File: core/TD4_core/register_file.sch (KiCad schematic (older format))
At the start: 12 parts

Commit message: Started refactoring
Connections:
- net In_0 renamed In0
- net In_1 renamed In1
- net In_2 renamed In2
- net In_3 renamed In3
- net Out_A_0 renamed A0
- net Out_A_1 renamed A1
- net Out_A_2 renamed A2
- net Out_A_3 renamed A3
- net Out_B_0 renamed B0
- net Out_B_1 renamed B1
- net Out_B_2 renamed B2
- net Out_B_3 renamed B3
- net Out_OUT_0 renamed OUT0
- net Out_OUT_1 renamed OUT1
- net Out_OUT_2 renamed OUT2
- net Out_OUT_3 renamed OUT3
- net Out_PC_0 renamed PC0
- net Out_PC_1 renamed PC1
- net Out_PC_2 renamed PC2
- net Out_PC_3 renamed PC3
- net Reg_sel_0 renamed Reg_sel0
- net Reg_sel_1 renamed Reg_sel1
- net Reg_sel_2 renamed Reg_sel2
- net Reg_sel_3 renamed Reg_sel3
- net nRESET renamed ~RESET
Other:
- note removed: "Reset & Clock"

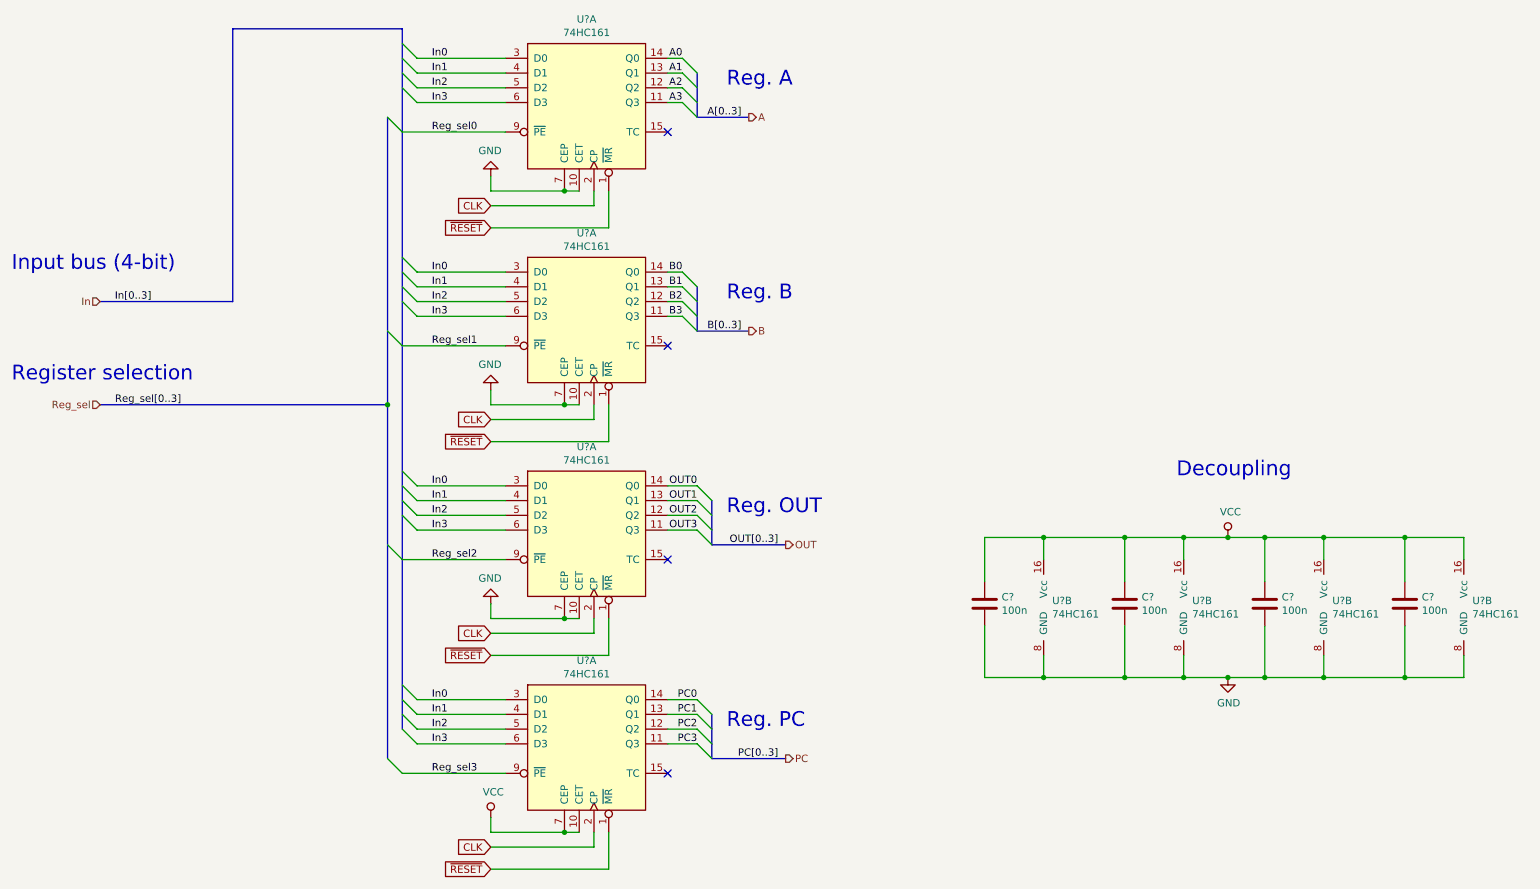
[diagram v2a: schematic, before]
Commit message: Main core schematic done; only decoder left
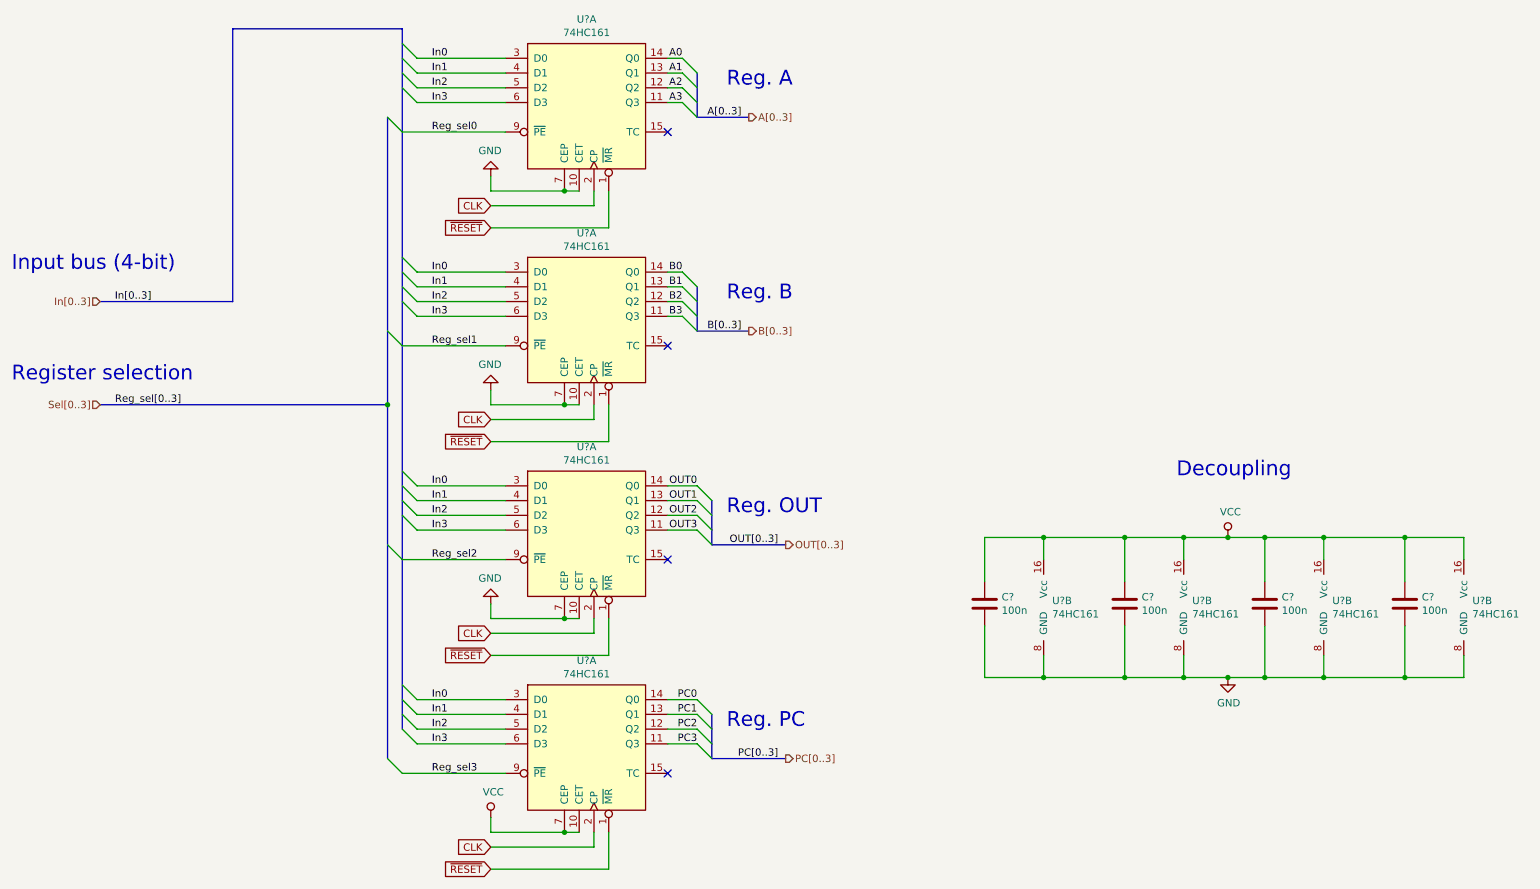
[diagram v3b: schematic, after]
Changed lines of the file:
@@
 $Descr A4 11693 8268
 encoding utf-8
-Sheet 2 6
+Sheet 2 9
 Title "TD4 core module"
 Date ""
@@
 Decoupling
 Text HLabel 5500 1850 2    50   Output ~ 0
-A
+A[0..3]
 Entry Wire Line
 	5050 2900 5150 3000
@@
 	4950 3200 5050 3200
 Text HLabel 5500 3300 2    50   Output ~ 0
-B
+B[0..3]
 Entry Wire Line
 	5150 4350 5250 4450
@@
 	4950 4650 5150 4650
 Text HLabel 5750 4750 2    50   Output ~ 0
-OUT
+OUT[0..3]
 Entry Wire Line
 	5150 5800 5250 5900
@@
 	4950 6100 5150 6100
 Text HLabel 5750 6200 2    50   Output ~ 0
-PC
+PC[0..3]
 Wire Wire Line
 	3750 3900 4450 3900
@@
 	3050 3800 1100 3800
 Text HLabel 1100 3800 0    50   Input ~ 0
-Reg_sel
+Sel[0..3]
 Text Label 1650 3800 2    50   ~ 0
 Reg_sel[0..3]
@@
 In[0..3]
 Text HLabel 1100 3100 0    50   Input ~ 0
-In
+In[0..3]
 Wire Wire Line
 	3250 2900 3850 2900

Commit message: Core assembled; decoder left
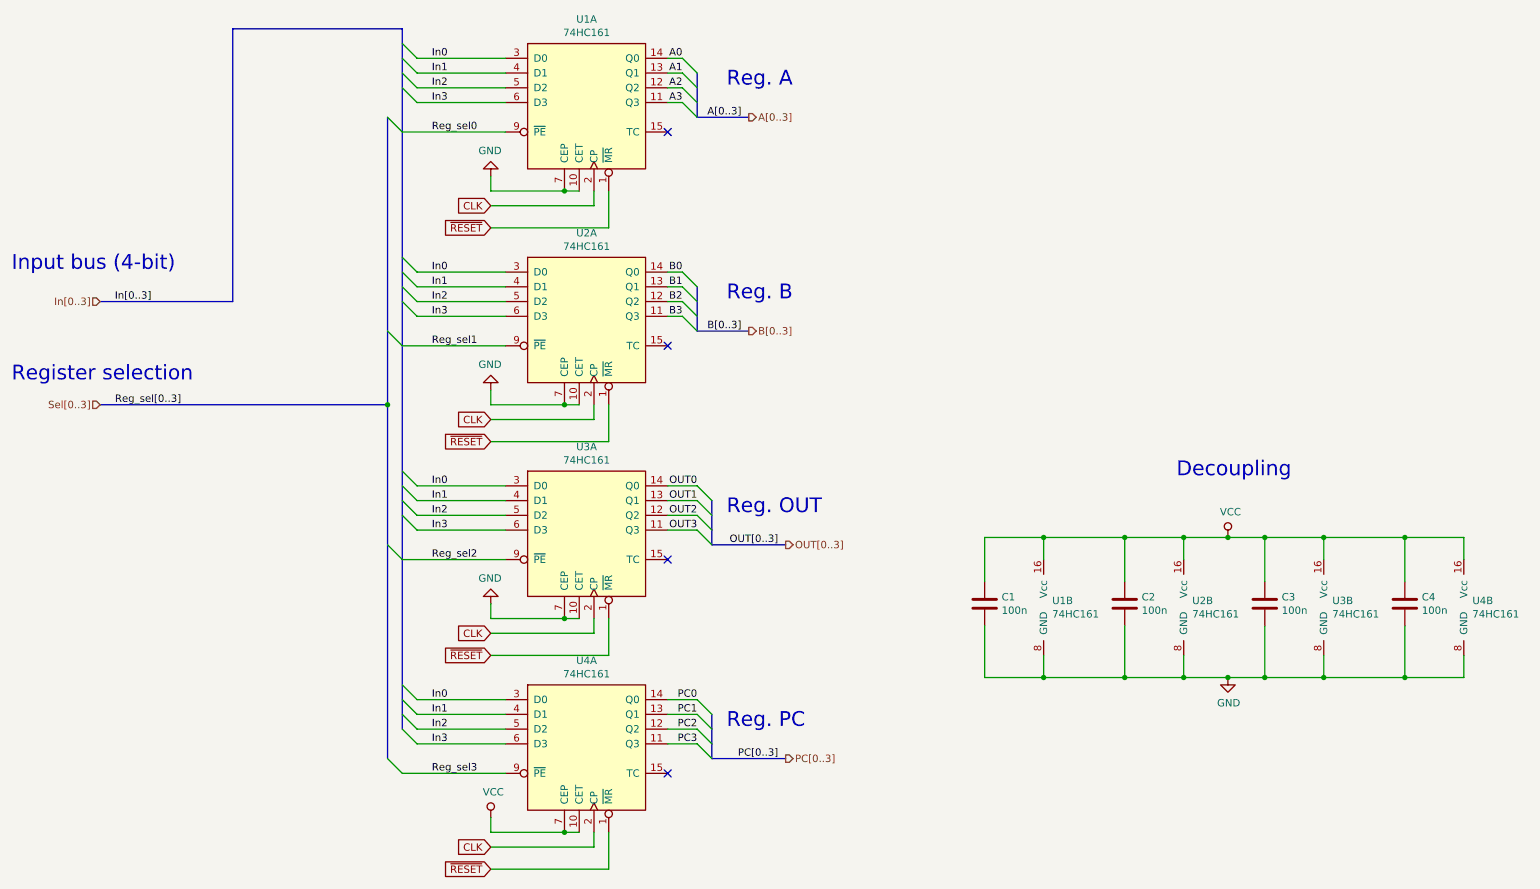
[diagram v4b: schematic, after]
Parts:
- gave numbers to parts that had none: 8
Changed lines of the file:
@@
 P 4400 1800
 AR Path="/5C597F7D" Ref="U?"  Part="1"
-AR Path="/5C594EF5/5C597F7D" Ref="U?"  Part="1"
-F 0 "U?" H 4400 2415 50  0000 C CNN
+AR Path="/5C594EF5/5C597F7D" Ref="U1"  Part="1"
+F 0 "U1" H 4400 2415 50  0000 C CNN
 F 1 "74HC161" H 4400 2324 50  0000 C CNN
 F 2 "Package_SO:SOIC-16_3.9x9.9mm_P1.27mm" H 3400 50  50  0001 C CNN
@@
 P 7500 5200
 AR Path="/5C598049" Ref="U?"  Part="2"
-AR Path="/5C594EF5/5C598049" Ref="U?"  Part="2"
-F 0 "U?" H 7558 5271 50  0000 L CNN
+AR Path="/5C594EF5/5C598049" Ref="U1"  Part="2"
+F 0 "U1" H 7558 5271 50  0000 L CNN
 F 1 "74HC161" H 7558 5180 50  0000 L CNN
 F 2 "Package_SO:SOIC-16_3.9x9.9mm_P1.27mm" H 6500 3450 50  0001 C CNN
@@
 P 4400 3250
 AR Path="/5C5981EC" Ref="U?"  Part="1"
-AR Path="/5C594EF5/5C5981EC" Ref="U?"  Part="1"
-F 0 "U?" H 4400 3865 50  0000 C CNN
+AR Path="/5C594EF5/5C5981EC" Ref="U2"  Part="1"
+F 0 "U2" H 4400 3865 50  0000 C CNN
 F 1 "74HC161" H 4400 3774 50  0000 C CNN
 F 2 "Package_SO:SOIC-16_3.9x9.9mm_P1.27mm" H 3400 1500 50  0001 C CNN
@@
 P 4400 4700
 AR Path="/5C598244" Ref="U?"  Part="1"
-AR Path="/5C594EF5/5C598244" Ref="U?"  Part="1"
-F 0 "U?" H 4400 5315 50  0000 C CNN
+AR Path="/5C594EF5/5C598244" Ref="U3"  Part="1"
+F 0 "U3" H 4400 5315 50  0000 C CNN
 F 1 "74HC161" H 4400 5224 50  0000 C CNN
 F 2 "Package_SO:SOIC-16_3.9x9.9mm_P1.27mm" H 3400 2950 50  0001 C CNN
@@
 P 8450 5200
 AR Path="/5C59842E" Ref="U?"  Part="2"
-AR Path="/5C594EF5/5C59842E" Ref="U?"  Part="2"
-F 0 "U?" H 8508 5271 50  0000 L CNN
+AR Path="/5C594EF5/5C59842E" Ref="U2"  Part="2"
+F 0 "U2" H 8508 5271 50  0000 L CNN
 F 1 "74HC161" H 8508 5180 50  0000 L CNN
 F 2 "Package_SO:SOIC-16_3.9x9.9mm_P1.27mm" H 7450 3450 50  0001 C CNN
@@
 P 9400 5200
 AR Path="/5C598474" Ref="U?"  Part="2"
-AR Path="/5C594EF5/5C598474" Ref="U?"  Part="2"
-F 0 "U?" H 9458 5271 50  0000 L CNN
+AR Path="/5C594EF5/5C598474" Ref="U3"  Part="2"
+F 0 "U3" H 9458 5271 50  0000 L CNN
 F 1 "74HC161" H 9458 5180 50  0000 L CNN
 F 2 "Package_SO:SOIC-16_3.9x9.9mm_P1.27mm" H 8400 3450 50  0001 C CNN
@@
 P 10350 5200
 AR Path="/5C5984B8" Ref="U?"  Part="2"
-AR Path="/5C594EF5/5C5984B8" Ref="U?"  Part="2"
-F 0 "U?" H 10408 5271 50  0000 L CNN
+AR Path="/5C594EF5/5C5984B8" Ref="U4"  Part="2"
+F 0 "U4" H 10408 5271 50  0000 L CNN
 F 1 "74HC161" H 10408 5180 50  0000 L CNN
 F 2 "Package_SO:SOIC-16_3.9x9.9mm_P1.27mm" H 9350 3450 50  0001 C CNN
@@
 NoConn ~ 4950 6300
 $Comp
-L power:GND #PWR?
+L power:GND #PWR0103
 U 1 1 5C5ACD50
 P 3750 2250
-F 0 "#PWR?" H 3750 2000 50  0001 C CNN
+F 0 "#PWR0103" H 3750 2000 50  0001 C CNN
 F 1 "GND" H 3755 2077 50  0000 C CNN
 F 2 "" H 3750 2250 50  0001 C CNN
@@
 	4250 5250 3750 5250
 $Comp
-L power:GND #PWR?
+L power:GND #PWR0104
 U 1 1 5C5B437D
 P 3750 3700
-F 0 "#PWR?" H 3750 3450 50  0001 C CNN
+F 0 "#PWR0104" H 3750 3450 50  0001 C CNN
 F 1 "GND" H 3755 3527 50  0000 C CNN
 F 2 "" H 3750 3700 50  0001 C CNN
@@
 	3750 3700 3750 3800
 $Comp
-L power:GND #PWR?
+L power:GND #PWR0105
 U 1 1 5C5B4E91
 P 3750 5150
-F 0 "#PWR?" H 3750 4900 50  0001 C CNN
+F 0 "#PWR0105" H 3750 4900 50  0001 C CNN
 F 1 "GND" H 3755 4977 50  0000 C CNN
 F 2 "" H 3750 5150 50  0001 C CNN
@@
 	3750 6600 3750 6700
 $Comp
-L power:VCC #PWR?
+L power:VCC #PWR0106
 U 1 1 5C5B65A8
 P 3750 6600
-F 0 "#PWR?" H 3750 6450 50  0001 C CNN
+F 0 "#PWR0106" H 3750 6450 50  0001 C CNN
 F 1 "VCC" H 3767 6773 50  0000 C CNN
 F 2 "" H 3750 6600 50  0001 C CNN
@@
 	4950 1750 5050 1750
 $Comp
-L power:VCC #PWR?
+L power:VCC #PWR0107
 U 1 1 5C5F640A
 P 8750 4700
-F 0 "#PWR?" H 8750 4550 50  0001 C CNN
+F 0 "#PWR0107" H 8750 4550 50  0001 C CNN
 F 1 "VCC" H 8767 4873 50  0000 C CNN
 F 2 "" H 8750 4700 50  0001 C CNN
@@
 $EndComp
 $Comp
-L Device:C C?
+L Device:C C1
 U 1 1 5C5FA440
 P 7100 5150
-F 0 "C?" H 7215 5196 50  0000 L CNN
+F 0 "C1" H 7215 5196 50  0000 L CNN
 F 1 "100n" H 7215 5105 50  0000 L CNN
 F 2 "" H 7138 5000 50  0001 C CNN
@@
 $EndComp
 $Comp
-L Device:C C?
+L Device:C C2
 U 1 1 5C5FA486
 P 8050 5150
-F 0 "C?" H 8165 5196 50  0000 L CNN
+F 0 "C2" H 8165 5196 50  0000 L CNN
 F 1 "100n" H 8165 5105 50  0000 L CNN
 F 2 "" H 8088 5000 50  0001 C CNN
@@
 $EndComp
 $Comp
-L Device:C C?
+L Device:C C4
 U 1 1 5C5FA4C0
 P 9950 5150
-F 0 "C?" H 10065 5196 50  0000 L CNN
+F 0 "C4" H 10065 5196 50  0000 L CNN
 F 1 "100n" H 10065 5105 50  0000 L CNN
 F 2 "" H 9988 5000 50  0001 C CNN
@@
 $EndComp
 $Comp
-L Device:C C?
+L Device:C C3
 U 1 1 5C5FA500
 P 9000 5150
-F 0 "C?" H 9115 5196 50  0000 L CNN
+F 0 "C3" H 9115 5196 50  0000 L CNN
 F 1 "100n" H 9115 5105 50  0000 L CNN
 F 2 "" H 9038 5000 50  0001 C CNN
@@
 	8750 4700 9000 4700
 $Comp
-L power:GND #PWR?
+L power:GND #PWR0108
 U 1 1 5C6635B5
 P 8750 5650
-F 0 "#PWR?" H 8750 5400 50  0001 C CNN
+F 0 "#PWR0108" H 8750 5400 50  0001 C CNN
 F 1 "GND" H 8755 5477 50  0000 C CNN
 F 2 "" H 8750 5650 50  0001 C CNN
@@
 P 4400 6150
 AR Path="/5C598292" Ref="U?"  Part="1"
-AR Path="/5C594EF5/5C598292" Ref="U?"  Part="1"
-F 0 "U?" H 4400 6765 50  0000 C CNN
+AR Path="/5C594EF5/5C598292" Ref="U4"  Part="1"
+F 0 "U4" H 4400 6765 50  0000 C CNN
 F 1 "74HC161" H 4400 6674 50  0000 C CNN
 F 2 "Package_SO:SOIC-16_3.9x9.9mm_P1.27mm" H 3400 4400 50  0001 C CNN

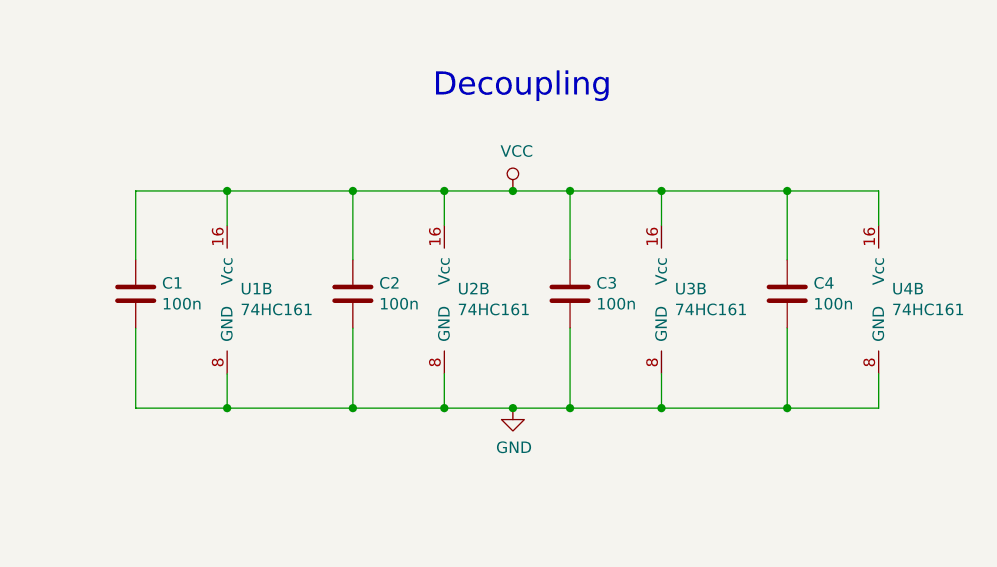
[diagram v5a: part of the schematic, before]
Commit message: Core schematic done. Backplane connector added, including separate .sch file to append.
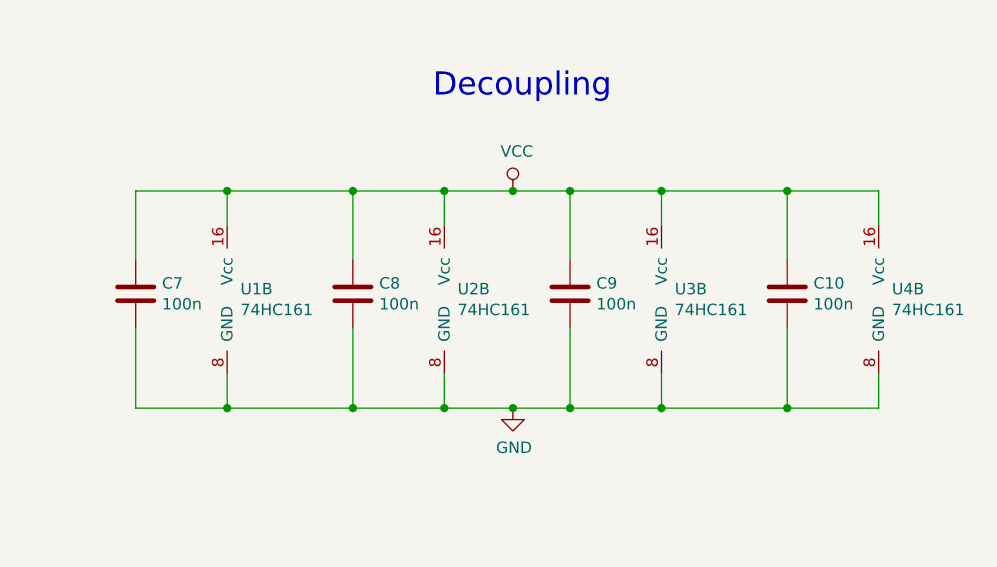
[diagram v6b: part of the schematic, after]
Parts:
- C10: renamed from C4; footprint (none) -> Capacitor_SMD:C_0805_2012Metric
- C7: renamed from C1; footprint (none) -> Capacitor_SMD:C_0805_2012Metric
- C8: renamed from C2; footprint (none) -> Capacitor_SMD:C_0805_2012Metric
- C9: renamed from C3; footprint (none) -> Capacitor_SMD:C_0805_2012Metric
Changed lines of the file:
@@
 NoConn ~ 4950 6300
 $Comp
-L power:GND #PWR03
+L power:GND #PWR017
 U 1 1 5C5ACD50
 P 3750 2250
-F 0 "#PWR03" H 3750 2000 50  0001 C CNN
+F 0 "#PWR017" H 3750 2000 50  0001 C CNN
 F 1 "GND" H 3755 2077 50  0000 C CNN
 F 2 "" H 3750 2250 50  0001 C CNN
@@
 	4250 5250 3750 5250
 $Comp
-L power:GND #PWR04
+L power:GND #PWR018
 U 1 1 5C5B437D
 P 3750 3700
-F 0 "#PWR04" H 3750 3450 50  0001 C CNN
+F 0 "#PWR018" H 3750 3450 50  0001 C CNN
 F 1 "GND" H 3755 3527 50  0000 C CNN
 F 2 "" H 3750 3700 50  0001 C CNN
@@
 	3750 3700 3750 3800
 $Comp
-L power:GND #PWR06
+L power:GND #PWR020
 U 1 1 5C5B4E91
 P 3750 5150
-F 0 "#PWR06" H 3750 4900 50  0001 C CNN
+F 0 "#PWR020" H 3750 4900 50  0001 C CNN
 F 1 "GND" H 3755 4977 50  0000 C CNN
 F 2 "" H 3750 5150 50  0001 C CNN
@@
 	3750 6600 3750 6700
 $Comp
-L power:VCC #PWR08
+L power:VCC #PWR022
 U 1 1 5C5B65A8
 P 3750 6600
-F 0 "#PWR08" H 3750 6450 50  0001 C CNN
+F 0 "#PWR022" H 3750 6450 50  0001 C CNN
 F 1 "VCC" H 3767 6773 50  0000 C CNN
 F 2 "" H 3750 6600 50  0001 C CNN
@@
 	4950 1750 5050 1750
 $Comp
-L power:VCC #PWR05
+L power:VCC #PWR019
 U 1 1 5C5F640A
 P 8750 4700
-F 0 "#PWR05" H 8750 4550 50  0001 C CNN
+F 0 "#PWR019" H 8750 4550 50  0001 C CNN
 F 1 "VCC" H 8767 4873 50  0000 C CNN
 F 2 "" H 8750 4700 50  0001 C CNN
@@
 $EndComp
 $Comp
-L Device:C C1
+L Device:C C7
 U 1 1 5C5FA440
 P 7100 5150
-F 0 "C1" H 7215 5196 50  0000 L CNN
+F 0 "C7" H 7215 5196 50  0000 L CNN
 F 1 "100n" H 7215 5105 50  0000 L CNN
-F 2 "" H 7138 5000 50  0001 C CNN
+F 2 "Capacitor_SMD:C_0805_2012Metric" H 7138 5000 50  0001 C CNN
 F 3 "~" H 7100 5150 50  0001 C CNN
 	1    7100 5150
@@
 $EndComp
 $Comp
-L Device:C C2
+L Device:C C8
 U 1 1 5C5FA486
 P 8050 5150
-F 0 "C2" H 8165 5196 50  0000 L CNN
+F 0 "C8" H 8165 5196 50  0000 L CNN
 F 1 "100n" H 8165 5105 50  0000 L CNN
-F 2 "" H 8088 5000 50  0001 C CNN
+F 2 "Capacitor_SMD:C_0805_2012Metric" H 8088 5000 50  0001 C CNN
 F 3 "~" H 8050 5150 50  0001 C CNN
 	1    8050 5150
@@
 $EndComp
 $Comp
-L Device:C C4
+L Device:C C10
 U 1 1 5C5FA4C0
 P 9950 5150
-F 0 "C4" H 10065 5196 50  0000 L CNN
+F 0 "C10" H 10065 5196 50  0000 L CNN
 F 1 "100n" H 10065 5105 50  0000 L CNN
-F 2 "" H 9988 5000 50  0001 C CNN
+F 2 "Capacitor_SMD:C_0805_2012Metric" H 9988 5000 50  0001 C CNN
 F 3 "~" H 9950 5150 50  0001 C CNN
 	1    9950 5150
@@
 $EndComp
 $Comp
-L Device:C C3
+L Device:C C9
 U 1 1 5C5FA500
 P 9000 5150
-F 0 "C3" H 9115 5196 50  0000 L CNN
+F 0 "C9" H 9115 5196 50  0000 L CNN
 F 1 "100n" H 9115 5105 50  0000 L CNN
-F 2 "" H 9038 5000 50  0001 C CNN
+F 2 "Capacitor_SMD:C_0805_2012Metric" H 9038 5000 50  0001 C CNN
 F 3 "~" H 9000 5150 50  0001 C CNN
 	1    9000 5150
@@
 	8750 4700 9000 4700
 $Comp
-L power:GND #PWR07
+L power:GND #PWR021
 U 1 1 5C6635B5
 P 8750 5650
-F 0 "#PWR07" H 8750 5400 50  0001 C CNN
+F 0 "#PWR021" H 8750 5400 50  0001 C CNN
 F 1 "GND" H 8755 5477 50  0000 C CNN
 F 2 "" H 8750 5650 50  0001 C CNN
